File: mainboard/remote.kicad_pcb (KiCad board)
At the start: 2 copper layers, 185.4 x 109 mm, 44 parts, among them J1 Conn_01x02, J10 Conn_01x03, J11 Conn_01x03, J12 Conn_01x02, J13 Conn_01x04, J14 Conn_01x04, J2 Conn_01x02, J5 Conn_01x02, J6 Conn_01x02, SW1 SW_SPDT_MSM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

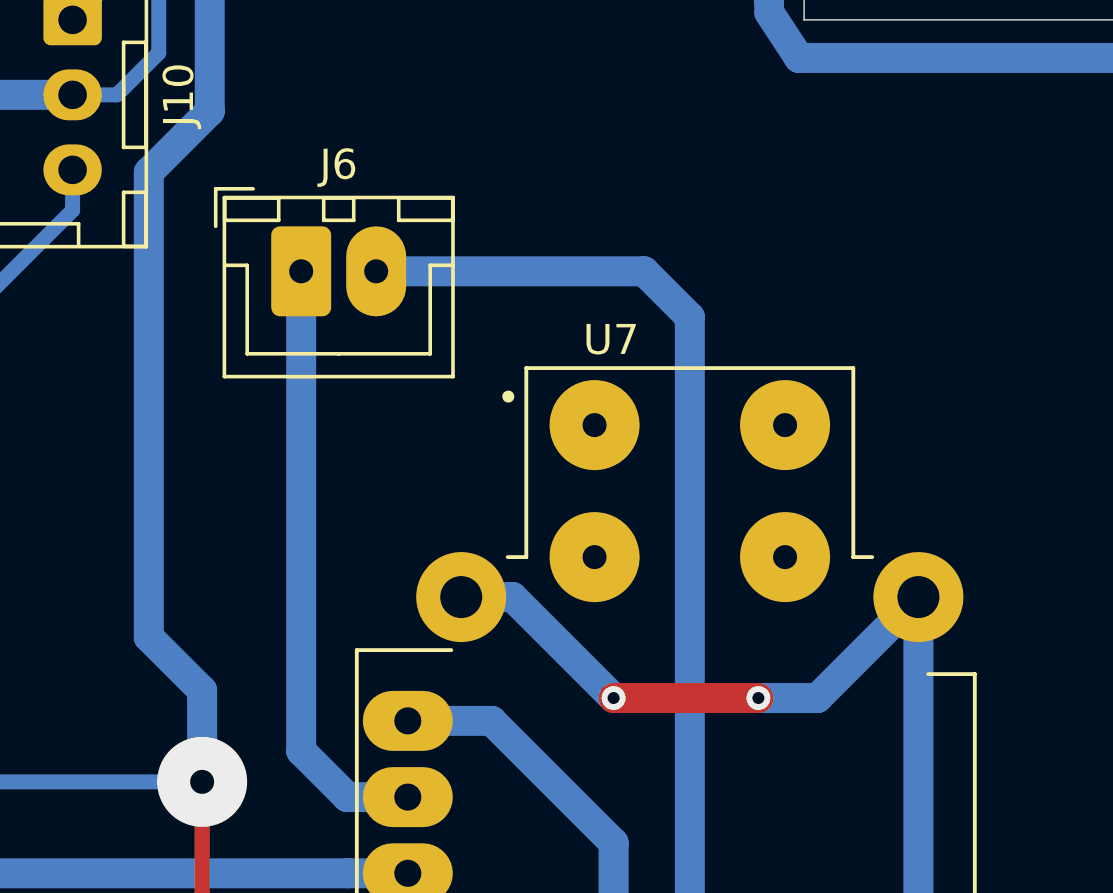
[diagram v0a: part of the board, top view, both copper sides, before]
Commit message: Move jumper.
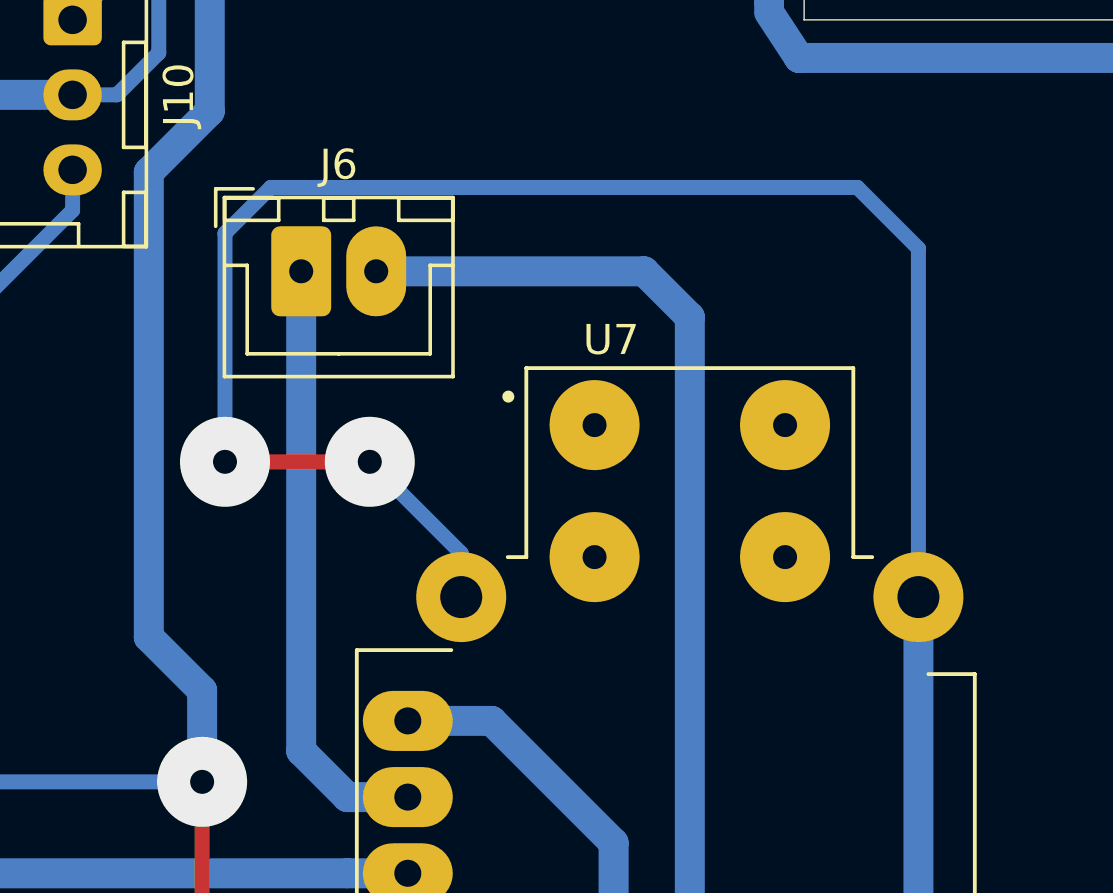
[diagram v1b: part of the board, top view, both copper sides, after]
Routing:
- net GND: track 628.9 -> 665.3 mm
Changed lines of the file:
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@@
     (thickness 1.6)
     (drawings 2593)
-    (tracks 359)
+    (tracks 362)
     (zones 0)
     (modules 44)
@@
   )
   (setup
-    (last_trace_width 0.25)
+    (last_trace_width 0.5)
     (user_trace_width 0.5)
     (user_trace_width 0.8)
@@
   (segment (start 56.27 172.466) (end 55.372 171.568) (width 1) (layer B.Cu) (net 1))
   (segment (start 62.738 172.466) (end 56.27 172.466) (width 1) (layer B.Cu) (net 1))
-  (via (at 83.82 214.122) (size 0.8) (drill 0.4) (layers F.Cu B.Cu) (net 1))
-  (segment (start 78.74 210.7565) (end 80.4545 210.7565) (width 1) (layer B.Cu) (net 1))
-  (segment (start 80.4545 210.7565) (end 83.82 214.122) (width 1) (layer B.Cu) (net 1))
-  (via (at 88.646 214.122) (size 0.8) (drill 0.4) (layers F.Cu B.Cu) (net 1))
-  (segment (start 83.82 214.122) (end 88.646 214.122) (width 1) (layer F.Cu) (net 1))
-  (segment (start 90.6145 214.122) (end 93.98 210.7565) (width 1) (layer B.Cu) (net 1))
-  (segment (start 88.646 214.122) (end 90.6145 214.122) (width 1) (layer B.Cu) (net 1))
   (segment (start 124.46 212.23) (end 127 212.23) (width 1) (layer B.Cu) (net 1))
   (segment (start 124.46 217.835) (end 124.46 220.835) (width 1) (layer B.Cu) (net 1))
@@
   (segment (start 90.8475 227.224) (end 93.98 224.0915) (width 1) (layer B.Cu) (net 1))
   (segment (start 88.9 227.224) (end 90.8475 227.224) (width 1) (layer B.Cu) (net 1))
+  (via (at 75.692 206.248) (size 3) (drill 0.8) (layers F.Cu B.Cu) (net 1))
+  (segment (start 78.74 210.7565) (end 78.74 209.296) (width 0.5) (layer B.Cu) (net 1))
+  (segment (start 78.74 209.296) (end 75.692 206.248) (width 0.5) (layer B.Cu) (net 1))
+  (via (at 70.866 206.248) (size 3) (drill 0.8) (layers F.Cu B.Cu) (net 1))
+  (segment (start 75.692 206.248) (end 70.866 206.248) (width 0.5) (layer F.Cu) (net 1))
+  (segment (start 70.866 206.248) (end 70.866 198.628) (width 0.5) (layer B.Cu) (net 1))
+  (segment (start 70.866 198.628) (end 72.39 197.104) (width 0.5) (layer B.Cu) (net 1))
+  (segment (start 72.39 197.104) (end 91.948 197.104) (width 0.5) (layer B.Cu) (net 1))
+  (segment (start 93.98 199.136) (end 93.98 210.7565) (width 0.5) (layer B.Cu) (net 1))
+  (segment (start 91.948 197.104) (end 93.98 199.136) (width 0.5) (layer B.Cu) (net 1))
   (segment (start 179.2455 135.128) (end 182.118 135.128) (width 1) (layer B.Cu) (net 2))
   (segment (start 193.294 188.468) (end 194.31 187.452) (width 0.5) (layer B.Cu) (net 2))

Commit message: Order PCB.
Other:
- net class Default removed
